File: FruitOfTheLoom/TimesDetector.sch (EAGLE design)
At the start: 0 parts

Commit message: Creacion de proyecto detector de tiempo y creacion de librerias - modulo de micro sd (solo el contorno y conexion)
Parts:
- added B1: SPARKFUN_PRO_MICRO, SparkFun-Boards:SPARKFUN_PRO_MICRO
- added J1: (no value), SparkFun-Connectors:CONN_05X2SHD

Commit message: ordenamiento y conexion
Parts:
- added C1: (no value), capacitor-wima:C10/6
- added FRAME1: FRAME-LETTER, SparkFun-Aesthetics:FRAME-LETTER
- added J2, J3, J4, J5, J6, J7: (no value), SparkFun-Connectors:CONN_04POLAR
- added K1, K2: RELAY-SPDT-JZC-11F, SparkFun-Electromechanical:RELAY-SPDT-JZC-11F
- added MODULE1: MICROSD_SPARKFUN_LEVEL_SHIFTING_MODULE, MODULOS_MICROSD:MICROSD_SPARKFUN_LEVEL_SHIFTING_MODULE
- added R1, R2, R3, R4, R5, R6, R7: (no value), SparkFun-Resistors:RESISTORAXIAL-0.3
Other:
- note added: "Supply"
- moved on the sheet: B1, J1

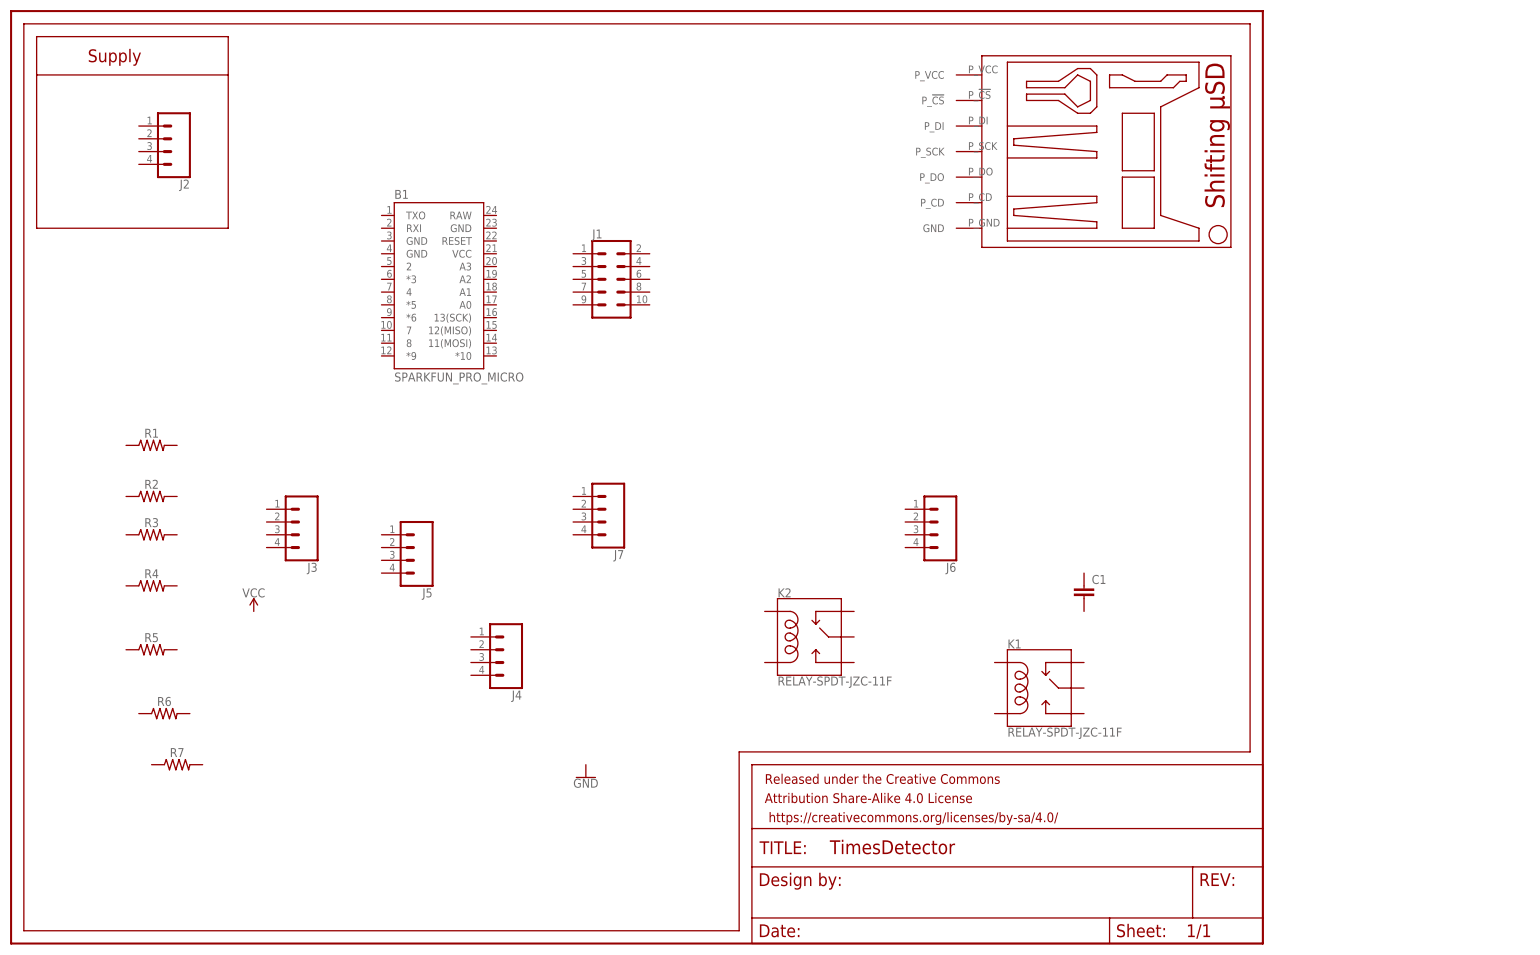
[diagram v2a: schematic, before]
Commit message: Conexiones de circuitos, relay, led, boton1
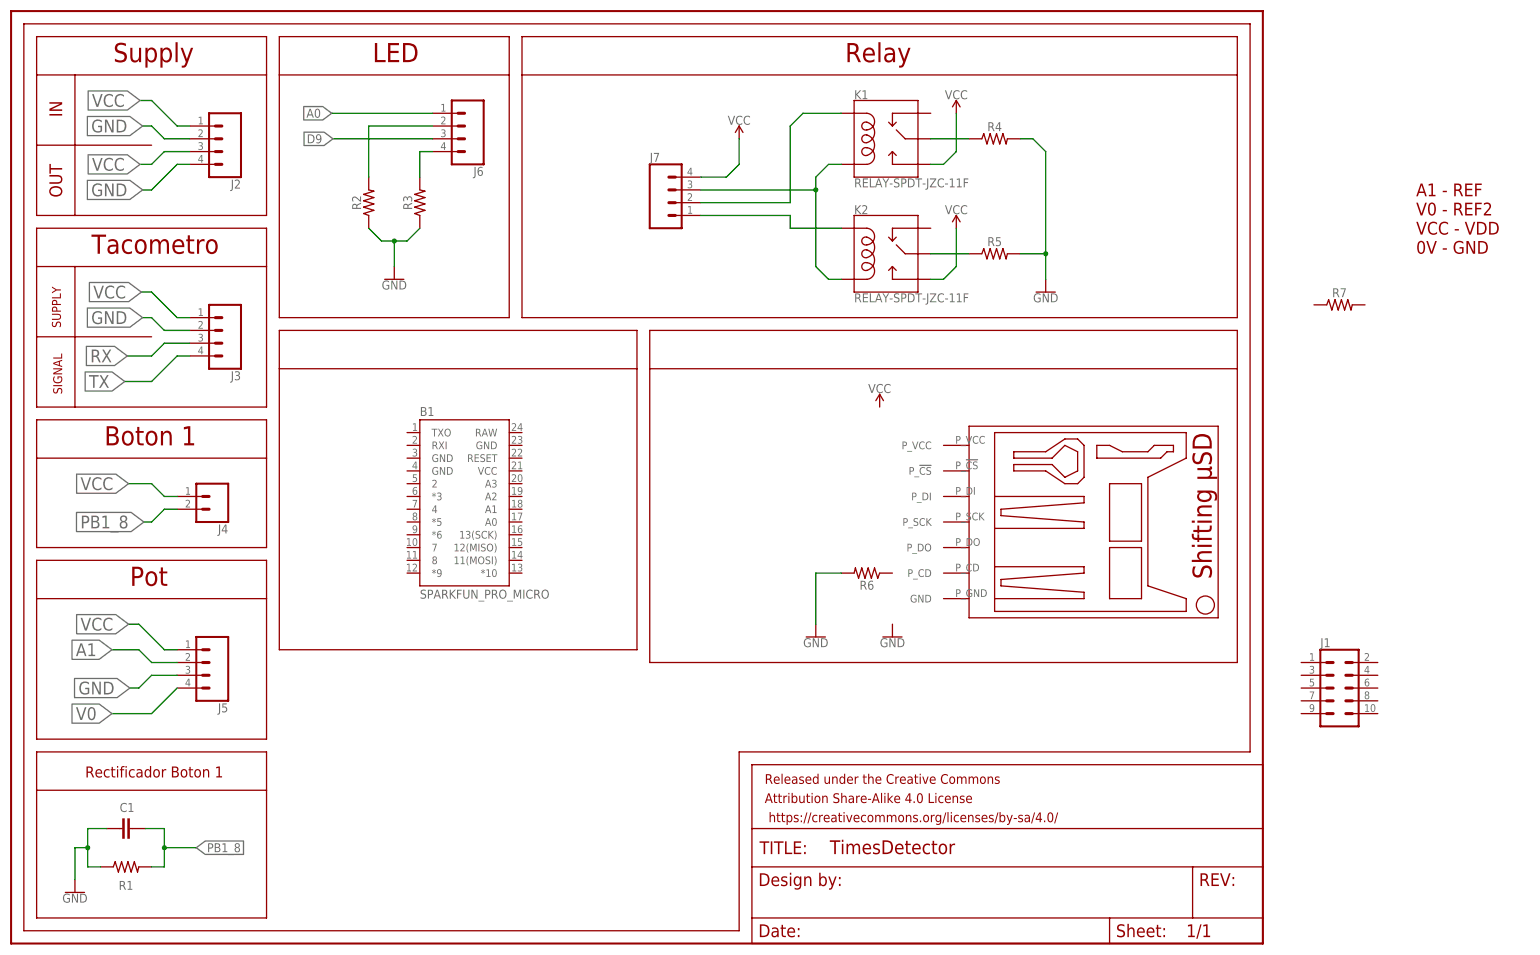
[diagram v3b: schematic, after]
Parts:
- J4: device SparkFun-Connectors:CONN_04POLAR -> SparkFun-Connectors:CONN_02POLAR
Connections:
- new net A0: J6.1
- new net A1: J5.2
- new net D9: J6.3
- new net GND: C1.2, J2.2, J2.4, J3.2, J5.3, R1.1, R2.1, R3.1, R4.2, R5.2, R6.2
- new net N$1: J7.3, K1.COIL2, K2.COIL2
- new net N$2: J6.4, R3.2
- new net N$3: K2.MAIN, R5.1
- new net N$4: J6.2, R2.2
- new net N$5: K1.MAIN, R4.1
- new net N$8: J7.1, K2.COIL1
- new net N$9: J7.2, K1.COIL1
- new net PB1_8: C1.1, J4.2, R1.2
- new net RX: J3.3
- new net TX: J3.4
- new net V0: J5.4
- new net VCC: J2.1, J2.3, J3.1, J4.1, J5.1, J7.4, K1.NO, K2.NO
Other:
- note added: "A1 - REF V0 - REF2 VCC - VDD 0V - GND"
- note added: "Boton 1"
- note added: "IN"
- note added: "LED"
- note added: "OUT"
- note added: "Pot"
- note added: "Rectificador Boton 1"
- note added: "Relay"
- note added: "SIGNAL"
- note added: "SUPPLY"
- note added: "Tacometro"
- moved on the sheet: B1, C1, J1, J2, J3, J5, J6, J7, K1, K2, R1, R2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

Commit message: Finalizacion de esquematico, erc con aprobaciones de conexion, inicializacion de placa
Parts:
- C1: device capacitor-wima:C10/6 -> resistor:CPOL-EUE2,5-6E
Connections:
- net N$8 renamed IN_SEN_2
- net N$9 renamed IN_SEN_1
- removed net N$1: J7.3, K1.COIL2, K2.COIL2
- removed net N$3: K2.MAIN, R5.1
- removed net N$5: K1.MAIN, R4.1
- removed net PB1_8: C1.1, J4.2, R1.2
- new net A2: B1.A2, K1.MAIN, R4.1
- new net A3: B1.A3, K2.MAIN, R5.1
- new net D10: B1.*10, MODULE1.P_!CS
- new net D11: B1.11(MOSI), MODULE1.P_DI
- new net D12: B1.12(MISO), MODULE1.P_DO
- new net D13: B1.13(SCK), MODULE1.P_SCK
- new net D2: B1.2, J1.5
- new net D3: B1.*3, J1.6
- new net D4: B1.4, J1.7
- new net D5: B1.*5, J1.8
- new net D6: B1.*6, J1.4
- new net D7: B1.7, J1.3
- new net D8: B1.8, C1.+, J4.2, R1.2
- new net N$6: MODULE1.P_CD, R6.1
- new net N$8: J1.1, R7.2
- new net VCC_O: B1.VCC, J1.10, J2.3, J4.1, J5.1, K1.NO, K2.NO, MODULE1.P_VCC, R7.1
- net A0: now also B1.A0
- net A1: now also B1.A1
- net D9: now also B1.*9
- net GND: now also B1.GND, B1.GND@1, B1.GND@2, C1.-, J1.9, K1.COIL2, K2.COIL2, MODULE1.GND; no longer C1.2
- net RX: now also B1.RXI
- net TX: now also B1.TXO
- net V0: now also J1.2
- net VCC: now also B1.RAW; no longer J2.3, J4.1, J5.1, K1.NO, K2.NO
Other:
- note added: "0.1"
- note added: "Arduino Pro Micro"
- note added: "Base Cable Ribbon 2x5"
- note added: "Ing. Hector Mendez"
- note added: "Modulo MicroSD"
- note removed: "A1 - REF V0 - REF2 VCC - VDD 0V - GND"
- moved on the sheet: J1, J2, J7, K1, K2, R1, R4, R5, R6, R7

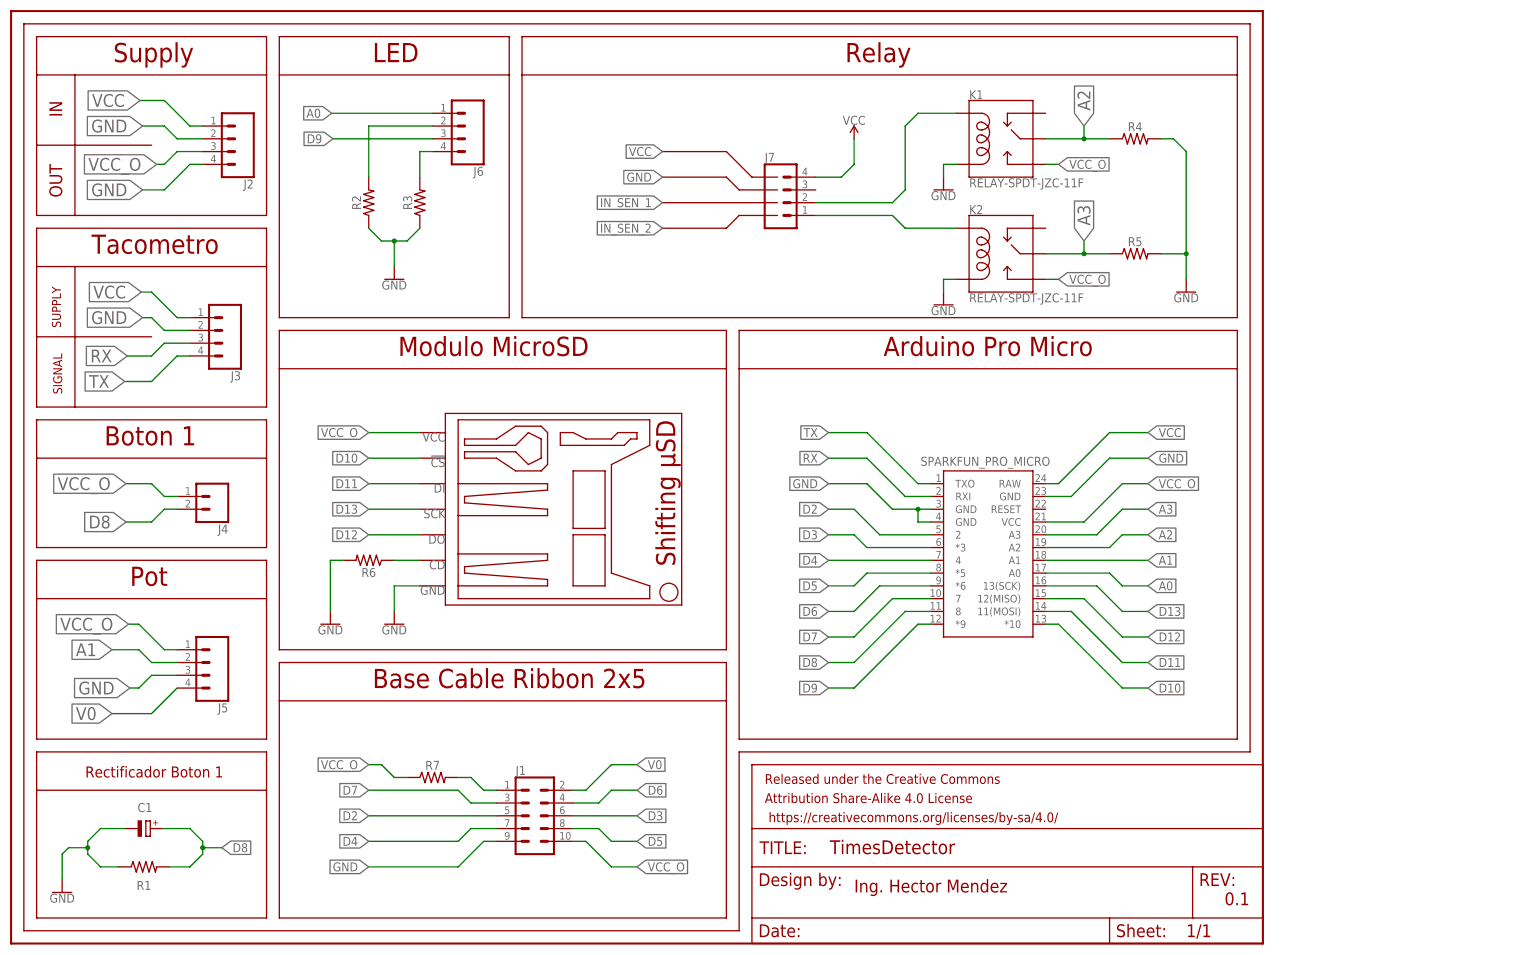
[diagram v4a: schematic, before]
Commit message: Finalizacion de esquematico, ordenamiento de diseño de placa electronica
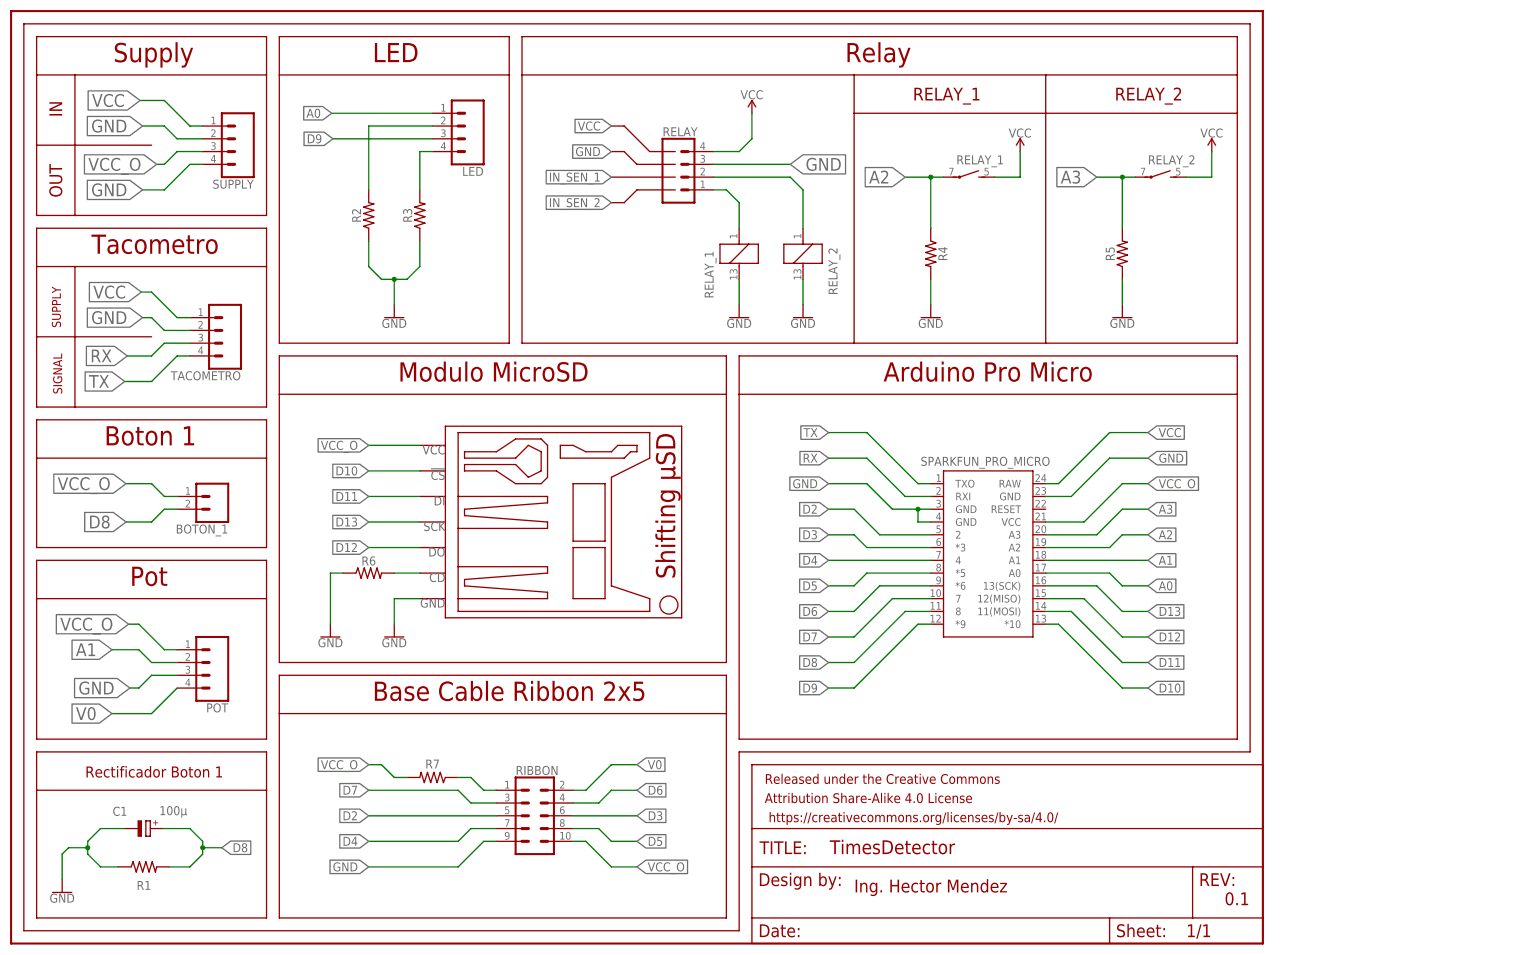
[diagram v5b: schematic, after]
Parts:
- removed J2, J3, J5, J6, J7: (no value), SparkFun-Connectors:CONN_04POLAR
- removed J4: (no value), SparkFun-Connectors:CONN_02POLAR
- removed K1, K2: RELAY-SPDT-JZC-11F, SparkFun-Electromechanical:RELAY-SPDT-JZC-11F
- added BOTON_1: (no value), SparkFun-Connectors:CONN_025MM
- added LED, POT, RELAY, SUPPLY, TACOMETRO: (no value), SparkFun-Connectors:CONN_04SCREW_LOCK
- added RELAY_1, RELAY_2: G6D-1A-ASI12VDC, relay:G6D-1A-ASI12VDC
- C1: value (none) -> 100µ
- renumbered J1 to RIBBON
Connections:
- removed net N$6: MODULE1.P_CD, R6.1
- new net N$1: MODULE1.P_CD, R6.2
- net A0: now also LED.1; no longer J6.1
- net A1: now also POT.2; no longer J5.2
- net A2: now also RELAY_12.P; no longer K1.MAIN
- net A3: now also R5.2, RELAY_22.P; no longer K2.MAIN, R5.1
- net D8: now also BOTON_1.2; no longer J4.2
- net D9: now also LED.3; no longer J6.3
- net GND: now also POT.3, R5.1, R6.1, RELAY.3, RELAY_11.2, RELAY_21.2, SUPPLY.2, SUPPLY.4, TACOMETRO.2; no longer J2.2, J2.4, J3.2, J5.3, K1.COIL2, K2.COIL2, R5.2, R6.2
- net IN_SEN_1: now also RELAY.2, RELAY_21.1; no longer J7.2, K1.COIL1
- net IN_SEN_2: now also RELAY.1, RELAY_11.1; no longer J7.1, K2.COIL1
- net N$2: now also LED.4; no longer J6.4
- net N$4: now also LED.2; no longer J6.2
- net N$8: now also R7.1; no longer R7.2
- net RX: now also TACOMETRO.3; no longer J3.3
- net TX: now also TACOMETRO.4; no longer J3.4
- net V0: now also POT.4; no longer J5.4
- net VCC: now also RELAY.4, RELAY_12.S, RELAY_22.S, SUPPLY.1, TACOMETRO.1; no longer J2.1, J3.1, J7.4
- net VCC_O: now also BOTON_1.1, POT.1, R7.2, SUPPLY.3; no longer J2.3, J4.1, J5.1, K1.NO, K2.NO, R7.1
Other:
- note added: "RELAY_1"
- note added: "RELAY_2"
- moved on the sheet: R2, R3, R4, R5, R6, R7

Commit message: Finalizacion de diseño de circuito, fase de revision
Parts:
- added FRAME3: FRAME-LETTERNO_PACKAGE, SparkFun-Aesthetics:FRAME-LETTERNO_PACKAGE
- added J2: (no value), SparkFun-Connectors:CONN_05PTH_LONGPADS
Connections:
- net D2: now also J2.5
- net D3: now also J2.4
- net D5: now also J2.3
- net D6: now also J2.2
- net D9: now also J2.1
